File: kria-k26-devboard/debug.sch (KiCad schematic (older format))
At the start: 68 parts, among them J8 USB4105-GF-A, J9 0878311420, Q10 DTC014TEBTL, Q17 DTC014TEBTL, Q9 DTC014TEBTL, U28 WE-TVS-82400152, U29 MIC5211-3.3YM6-TR, U30 FT4232HPQ, U31 93LC56CT-IMC, U32 74AVC4T245RSVRG4, U33 74AVC4T245RSVRG4, U34 SN74AVC2T245RSWR, U35 SN74AVC2T245RSWR, U36 NC7WZ07P6X, U54 TPD4E05U06QDQARQ1, Y5 ABM8G-12.000MHZ-18-D2Y-T

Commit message: Routed USB debug part, DP AUX, Supply for SD 3.0, improved decoupling. Other minor improvments
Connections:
- net USB_3V45 is gone; now on net VCC_USB: U34.1 (DIR2), U34.10 (DIR1)
- net FTDI_UARTB_RXD: now also U35.8 (A1); no longer U35.9 (A2)
- net FTDI_UARTB_TXD: now also U35.9 (A2); no longer U35.8 (A1)
- net GND: now also U35.1 (DIR2); no longer U35.10 (DIR1)
- net MIO36: now also U35.5 (B1); no longer U35.4 (B2)
- net MIO37: now also U35.4 (B2); no longer U35.5 (B1)
- net USB_PWRD_VCCIO: now also U35.10 (DIR1); no longer U35.1 (DIR2)
- net ~FTDI_PS_POR: now also U34.9 (A2); no longer U34.8 (A1)
- net ~FTDI_PS_SRST: now also U34.8 (A1); no longer U34.9 (A2)
- net ~PS_POR: now also U36.4 (Y2); no longer U36.6 (Y1)
- net ~PS_SRST_C2M: now also U36.6 (Y1); no longer U36.4 (Y2)
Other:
- note added: "A1 <- B"
- note removed: "A2 <- B"
- moved on the sheet: U28
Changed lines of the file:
@@
 Text Label 7400 5500 0    50   ~ 0
 FTDI_UARTB_RXD
+Text Label 11650 7950 2    50   ~ 0
+FTDI_UARTB_TXD
 Text Label 11650 7850 2    50   ~ 0
-FTDI_UARTB_TXD
-Text Label 11650 7950 2    50   ~ 0
 FTDI_UARTB_RXD
-Text Label 13250 8100 0    50   ~ 0
+Text Label 13250 8300 0    50   ~ 0
 USB_PWRD_VCCIO
-Wire Wire Line
-	13150 8100 13250 8100
 $Comp
 L power:GND #PWR0335
 U 1 1 6258C7A9
-P 13200 8300
-F 0 "#PWR0335" H 13200 8050 50  0001 C CNN
-F 1 "GND" H 13205 8127 50  0000 C CNN
-F 2 "" H 13200 8300 50  0001 C CNN
-F 3 "" H 13200 8300 50  0001 C CNN
-	1    13200 8300
-	1    0    0    -1
-$EndComp
-Wire Wire Line
-	13200 8300 13200 8200
+P 13350 8100
+F 0 "#PWR0335" H 13350 7850 50  0001 C CNN
+F 1 "GND" H 13355 7927 50  0000 C CNN
+F 2 "" H 13350 8100 50  0001 C CNN
+F 3 "" H 13350 8100 50  0001 C CNN
+	1    13350 8100
+	0    -1   -1   0
+$EndComp
 Wire Wire Line
 	13200 8200 13150 8200
@@
 	11650 8300 11650 8250
 Connection ~ 11650 8250
+Text HLabel 13150 7950 2    50   Input ~ 0
+MIO37
 Text HLabel 13150 7850 2    50   Input ~ 0
-MIO37
-Text HLabel 13150 7950 2    50   Input ~ 0
 MIO36
 Wire Wire Line
@@
 Wire Wire Line
 	14150 6100 13150 6100
-Text Label 13300 6250 0    50   ~ 0
-USB_3V45
 Wire Wire Line
 	13150 6250 13200 6250
@@
 Wire Wire Line
 	15450 6200 15350 6200
-Text HLabel 15450 6000 2    50   Input ~ 0
+Text HLabel 15450 6200 2    50   Input ~ 0
 ~PS_POR
 Wire Wire Line
@@
 Text Label 11650 6250 2    50   ~ 0
 ~FTDI_PWREN
+Text Label 11650 6100 2    50   ~ 0
+~FTDI_PS_POR
 Text Label 11650 6000 2    50   ~ 0
-~FTDI_PS_POR
-Text Label 11650 6100 2    50   ~ 0
 ~FTDI_PS_SRST
 Text Label 11700 1800 2    50   ~ 0
@@
 Text HLabel 1300 10250 0    50   Input ~ 0
 USBC_VBUS
-Wire Wire Line
-	1300 10250 1600 10250
 Text HLabel 7050 8200 2    50   Input ~ 0
 PD_EN
@@
 Text Notes 600  3550 0    100  ~ 20
 Decoupling and Filtering
-Text HLabel 15450 6200 2    50   Input ~ 0
+Text HLabel 15450 6000 2    50   Input ~ 0
 ~PS_SRST_C2M
 Text HLabel 9200 10600 0    50   Input ~ 0
@@
 A2 -> B
 Text Notes 12250 7850 0    50   ~ 0
-A1 -> B
+A1 <- B
 Text Notes 12250 7950 0    50   ~ 0
-A2 <- B
+A2 -> B
 Wire Wire Line
 	1850 3950 2100 3950
@@
 	1    0    0    -1
 $EndComp
-Text Label 2000 1250 0    50   ~ 0
-USBB_VBUS
 Connection ~ 1450 2850
 Wire Wire Line
@@
 	1450 2850 1350 2850
 Wire Wire Line
-	1450 2750 1450 2850
-Wire Wire Line
-	1350 2750 1450 2750
-Wire Wire Line
-	1400 2300 1350 2300
-Wire Wire Line
-	1350 2200 1400 2200
-Wire Wire Line
-	1400 2050 1350 2050
-Wire Wire Line
-	1350 1950 1400 1950
+	1400 2250 1350 2250
+Wire Wire Line
+	1350 2150 1400 2150
+Wire Wire Line
+	1400 2000 1350 2000
+Wire Wire Line
+	1350 1900 1400 1900
 $Comp
 L power:GND #PWR?
@@
 	1    0    0    -1
 $EndComp
-NoConn ~ 1350 2550
-NoConn ~ 1350 2450
+NoConn ~ 1350 2500
+NoConn ~ 1350 2400
 $Comp
 L antmicroCapacitorsmisc:C_100n_0402_50V C?
@@
 	1650 1250 1650 1300
 Wire Wire Line
-	1350 1500 1450 1500
-Wire Wire Line
 	1450 1250 1650 1250
 Wire Wire Line
-	1450 1250 1450 1500
+	1450 1250 1450 1400
 Connection ~ 1650 1250
 $Comp
@@
 	1    0    0    -1
 $EndComp
-Text Label 2300 2150 0    50   ~ 0
+Text Label 2300 2100 0    50   ~ 0
 USBB_N
-Text Label 2300 2050 0    50   ~ 0
+Text Label 2300 2000 0    50   ~ 0
 USBB_P
 $Comp
 L antmicroTVSDiodes:WE-TVS-82400152 U28
 U 1 1 62B05FE1
-P 1850 2100
-F 0 "U28" H 1800 2300 50  0000 R CNN
-F 1 "WE-TVS-82400152" H 2250 1900 50  0000 R CNN
-F 2 "antmicro-footprints:SOT-563" H 1850 1900 50  0001 C CNN
-F 3 "https://katalog.we-online.de/pbs/datasheet/82400102.pdf" H 1850 1850 50  0001 C CNN
-F 4 "82400152" H 1500 1700 50  0001 C CNN "MPN"
-F 5 "Würth Elektronik" H 1600 1800 50  0001 C CNN "Manufacturer"
-	1    1850 2100
+P 1850 2050
+F 0 "U28" H 1800 2250 50  0000 R CNN
+F 1 "WE-TVS-82400152" H 2250 1850 50  0000 R CNN
+F 2 "antmicro-footprints:SOT-563" H 1850 1850 50  0001 C CNN
+F 3 "https://katalog.we-online.de/pbs/datasheet/82400102.pdf" H 1850 1800 50  0001 C CNN
+F 4 "82400152" H 1500 1650 50  0001 C CNN "MPN"
+F 5 "Würth Elektronik" H 1600 1750 50  0001 C CNN "Manufacturer"
+	1    1850 2050
 	1    0    0    -1
 $EndComp
@@
 	1650 1600 1650 1650
 Wire Wire Line
+	1400 1900 1400 1950
+Wire Wire Line
+	1400 2150 1400 2200
+Wire Wire Line
+	1400 1950 1550 1950
+Connection ~ 1400 1950
+Wire Wire Line
 	1400 1950 1400 2000
 Wire Wire Line
+	1400 2200 1500 2200
+Wire Wire Line
+	1500 2200 1500 2150
+Wire Wire Line
+	1500 2150 1550 2150
+Connection ~ 1400 2200
+Wire Wire Line
 	1400 2200 1400 2250
-Wire Wire Line
-	1400 2000 1550 2000
-Connection ~ 1400 2000
-Wire Wire Line
-	1400 2000 1400 2050
-Wire Wire Line
-	1400 2250 1500 2250
-Wire Wire Line
-	1500 2250 1500 2200
-Wire Wire Line
-	1500 2200 1550 2200
-Connection ~ 1400 2250
-Wire Wire Line
-	1400 2250 1400 2300
 $Comp
 L power:GND #PWR?
 U 1 1 629FE016
-P 1450 2450
+P 1450 2400
 AR Path="/63C44BC2/629FE016" Ref="#PWR?"  Part="1"
 AR Path="/63C44BC2/62A9ECDC/629FE016" Ref="#PWR?"  Part="1"
 AR Path="/625B0244/629FE016" Ref="#PWR0306"  Part="1"
-F 0 "#PWR0306" H 1450 2200 50  0001 C CNN
-F 1 "GND" H 1455 2277 50  0000 C CNN
-F 2 "" H 1450 2450 50  0001 C CNN
-F 3 "" H 1450 2450 50  0001 C CNN
-	1    1450 2450
-	1    0    0    -1
-$EndComp
-Wire Wire Line
-	2150 2000 2250 2000
-Wire Wire Line
-	2150 2200 2250 2200
-Wire Wire Line
-	2150 2100 2200 2100
-Wire Wire Line
-	1450 2100 1450 2450
-Wire Wire Line
-	2250 2000 2250 2050
-Wire Wire Line
-	2250 2050 2300 2050
-Wire Wire Line
-	2250 2200 2250 2150
-Wire Wire Line
-	2250 2150 2300 2150
-Wire Wire Line
-	2200 2100 2200 1600
+F 0 "#PWR0306" H 1450 2150 50  0001 C CNN
+F 1 "GND" H 1455 2227 50  0000 C CNN
+F 2 "" H 1450 2400 50  0001 C CNN
+F 3 "" H 1450 2400 50  0001 C CNN
+	1    1450 2400
+	1    0    0    -1
+$EndComp
+Wire Wire Line
+	2150 1950 2250 1950
+Wire Wire Line
+	2150 2150 2250 2150
+Wire Wire Line
+	2150 2050 2200 2050
+Wire Wire Line
+	1450 2050 1450 2400
+Wire Wire Line
+	2250 1950 2250 2000
+Wire Wire Line
+	2250 2000 2300 2000
+Wire Wire Line
+	2250 2150 2250 2100
+Wire Wire Line
+	2250 2100 2300 2100
+Wire Wire Line
+	2200 2050 2200 1600
 Wire Wire Line
 	2200 1600 1950 1600
@@
 Wire Wire Line
 	1950 1250 1650 1250
-NoConn ~ 1350 1700
-NoConn ~ 1350 1800
-Wire Wire Line
-	1450 2100 1550 2100
+NoConn ~ 1350 1650
+NoConn ~ 1350 1750
+Wire Wire Line
+	1450 2050 1550 2050
 $Comp
 L antmicroTransistorsBipolarSingle:DTC014TEBTL Q9
@@
 Wire Wire Line
 	12150 9000 12300 9000
-Wire Bus Line
-	4700 6500 4700 6700
 Wire Wire Line
 	12650 9200 12650 9600
@@
 	1    0    0    -1
 $EndComp
+Wire Wire Line
+	1300 10250 1600 10250
+Connection ~ 2200 1600
+Wire Wire Line
+	2200 1600 2200 1550
+Wire Wire Line
+	1350 2650 1450 2650
+Wire Wire Line
+	1450 2650 1450 2750
+Wire Wire Line
+	1350 2750 1450 2750
+Connection ~ 1450 2750
+Wire Wire Line
+	1450 2750 1450 2850
+Wire Wire Line
+	1350 1400 1450 1400
+Connection ~ 1450 1400
+Wire Wire Line
+	1450 1400 1450 1500
+Wire Wire Line
+	1350 1500 1450 1500
+Text Label 2000 1250 0    50   ~ 0
+USBB_VBUS
+Wire Wire Line
+	13150 8100 13350 8100
+Wire Wire Line
+	13200 8200 13200 8300
+Wire Wire Line
+	13200 8300 13250 8300
+Text Label 13300 6250 0    50   ~ 0
+VCC_USB
+Wire Bus Line
+	4700 6500 4700 6700
 $EndSCHEMATC

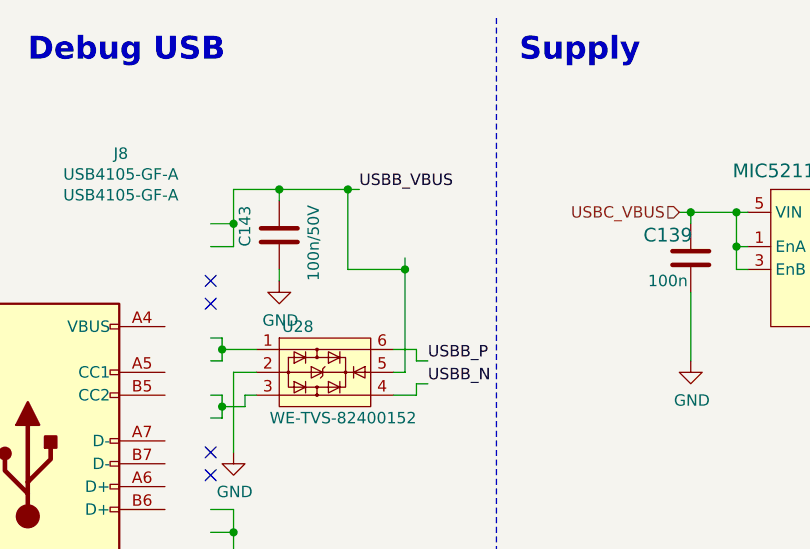
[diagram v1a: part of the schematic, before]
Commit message: Replaced PCIe clock generation (LVDS to HCSL), Clock component size optimization for USB, Optimized ESD protection for PD USB, placed and routed new clock circuitry, clock signals recalculated to 100Ohm  and re-routed
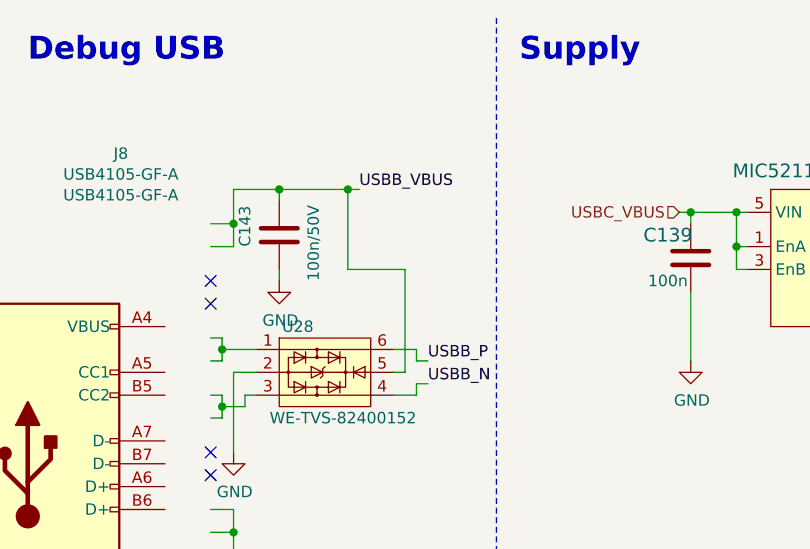
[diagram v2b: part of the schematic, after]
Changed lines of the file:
@@
 Wire Wire Line
 	1300 10250 1600 10250
-Connection ~ 2200 1600
-Wire Wire Line
-	2200 1600 2200 1550
 Wire Wire Line
 	1350 2650 1450 2650
